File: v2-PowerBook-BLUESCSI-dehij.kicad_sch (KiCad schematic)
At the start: 41 parts, among them J1 Micro_SD_Card, J2 Conn_02x20_Odd_Even, U1 YAAJ_BluePill_Part_Like

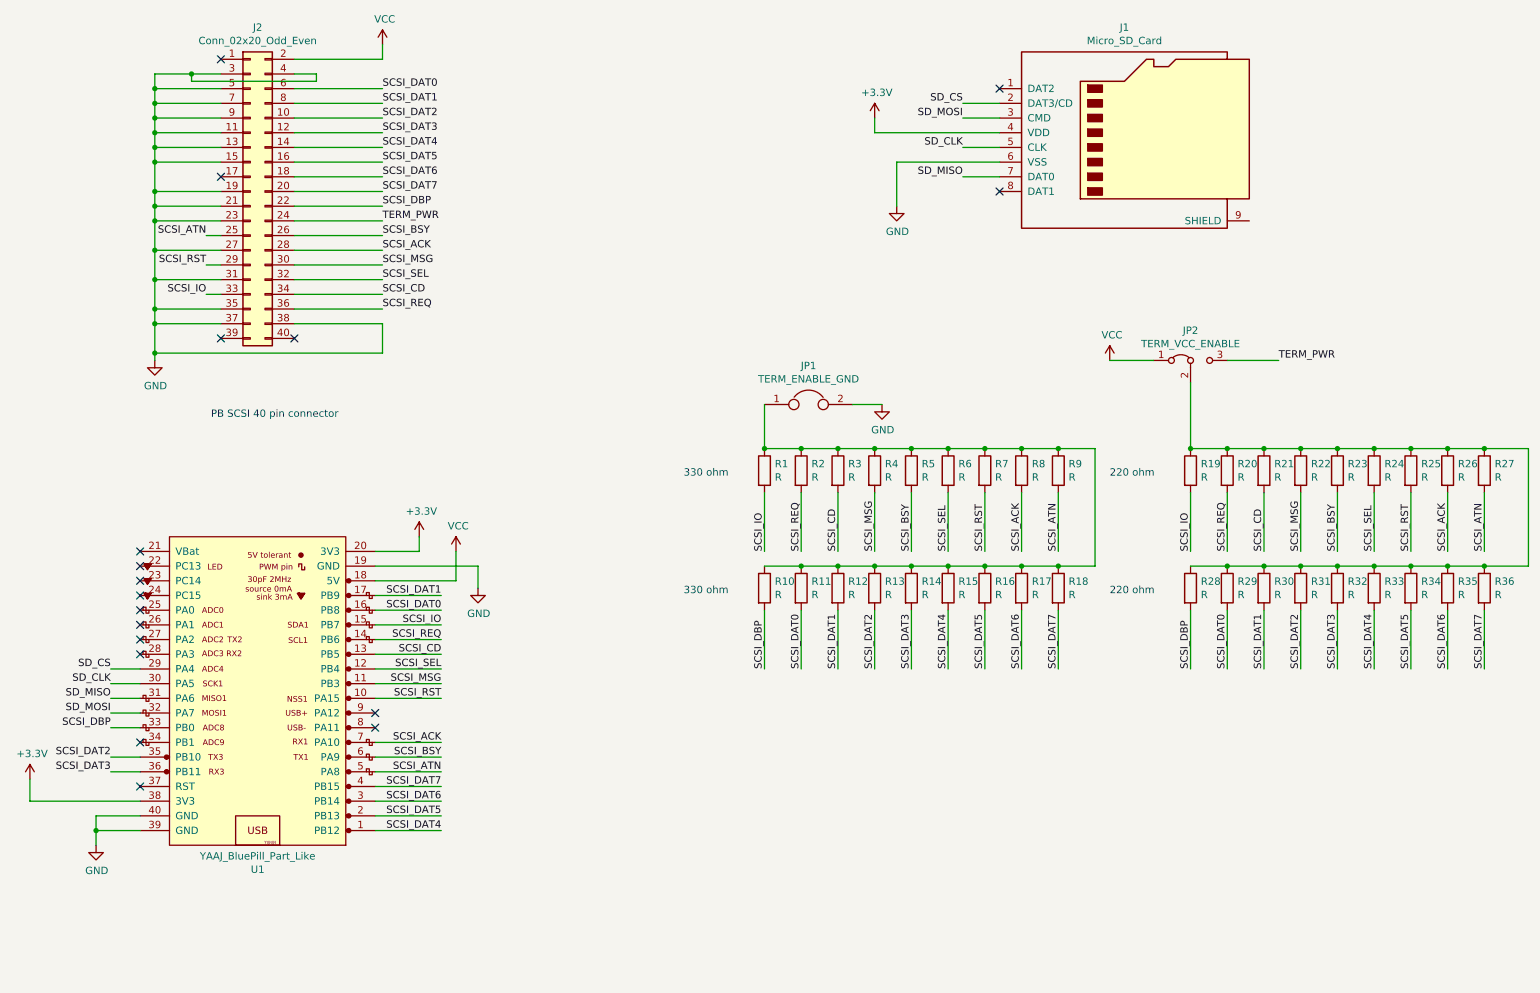
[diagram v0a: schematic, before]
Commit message: Updated layout for JLCPCB assembly
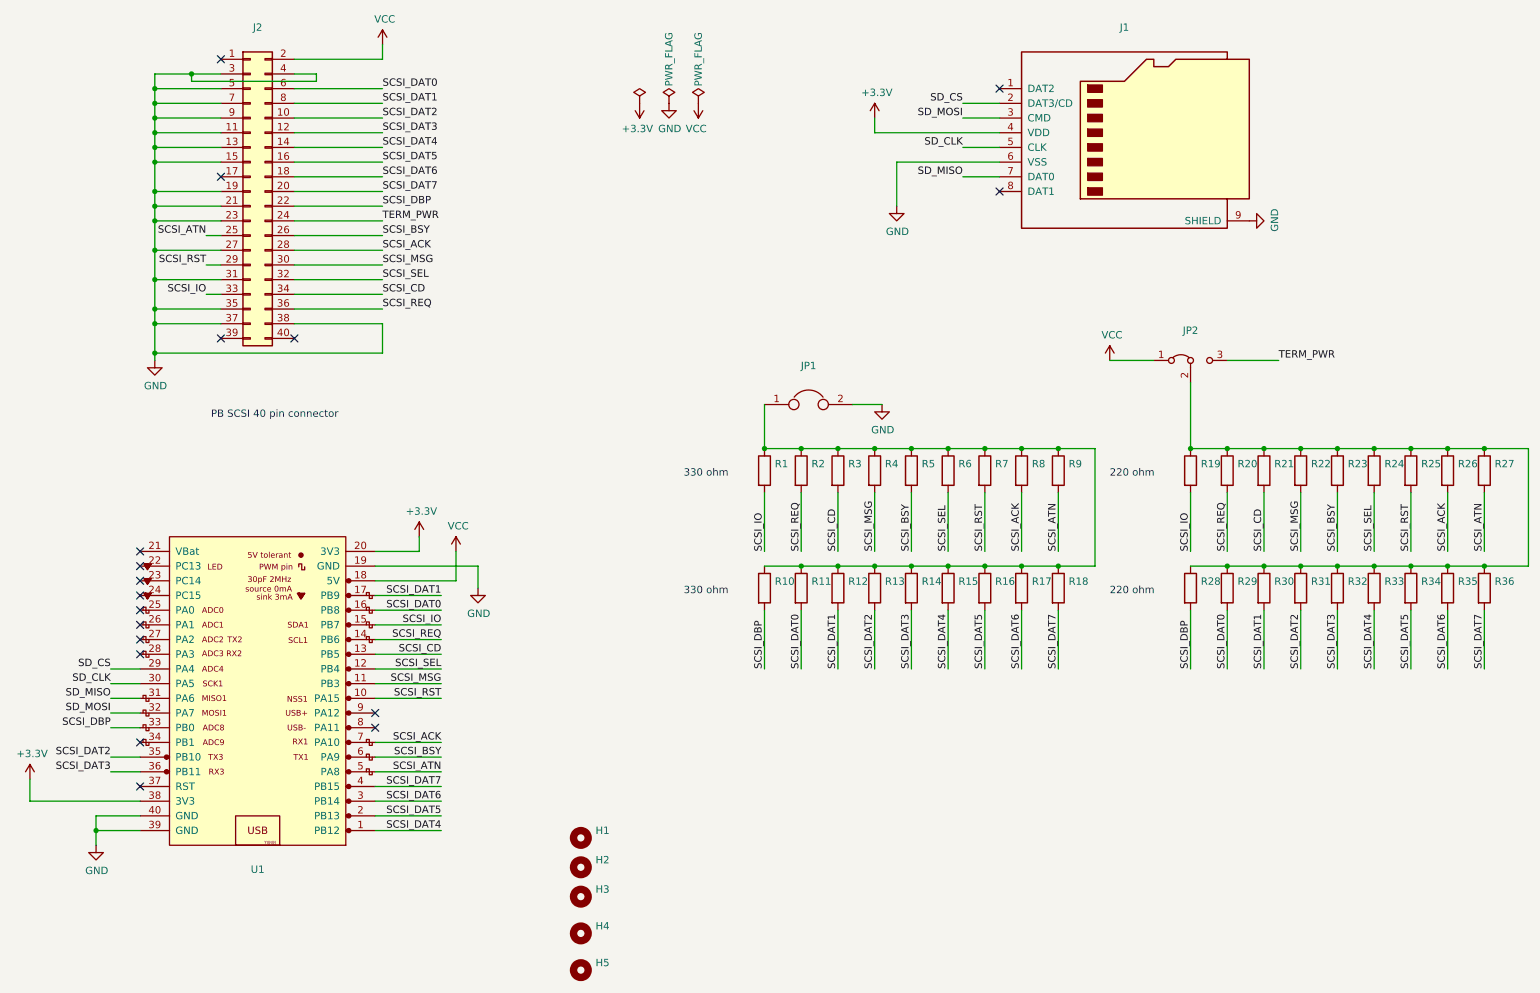
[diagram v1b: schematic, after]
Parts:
- added H1, H2, H3, H4, H5: (no value), symbol Mechanical:MountingHole
- J1: value Micro_SD_Card -> (none); footprint Other footprints:Conn_uSDcard -> (none); LCSC (none) -> C164170
- J2: value Conn_02x20_Odd_Even -> (none); footprint Connector_PinSocket_2.00mm:PinSocket_2x20_P2.00mm_Vertical -> (none)
- JP1: value TERM_ENABLE_GND -> (none); footprint Jumper:SolderJumper-2_P1.3mm_Bridged_Pad1.0x1.5mm -> (none)
- JP2: value TERM_VCC_ENABLE -> (none); footprint Jumper:SolderJumper-3_P1.3mm_Bridged12_Pad1.0x1.5mm_NumberLabels -> (none)
- R1, R10, R11, R12, R13, R14, R15, R16, R17, R18, R2, R3, R4, R5, R6, R7, R8, R9: value R -> (none); footprint Resistor_SMD:R_1206_3216Metric_Pad1.30x1.75mm_HandSolder -> (none); LCSC (none) -> C365291
- R19, R20, R21, R22, R23, R24, R25, R26, R27, R28, R29, R30, R31, R32, R33, R34, R35, R36: value R -> (none); footprint Resistor_SMD:R_1206_3216Metric_Pad1.30x1.75mm_HandSolder -> (none); LCSC (none) -> C163392
- U1: value YAAJ_BluePill_Part_Like -> (none); footprint Footprints:YAAJ_BluePill_2 -> (none)
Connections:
- net GND: now also J1.9 (SHIELD)
